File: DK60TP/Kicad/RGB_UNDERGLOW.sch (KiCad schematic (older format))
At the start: 0 parts

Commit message: - DK60TP: Added RGB underglow
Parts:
- added C12, C13, C14, C15, C16: 0.1u, Capacitors_SMD:C_0805_HandSoldering, symbol C_Small
- added D149, D150, D151, D152, D153: WS2812B, Footprint:WS2812B, symbol WS2812B
- added J2: 3PIN, Pin_Headers:Pin_Header_Straight_1x03, symbol 3PIN
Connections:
- new net: D149.2 (DOUT), D150.4 (DIN)
- new net: D150.2 (DOUT), D151.4 (DIN)
- new net: D151.2 (DOUT), D152.4 (DIN)
- new net: D152.2 (DOUT), D153.4 (DIN)
- new net DOUT: D153.2 (DOUT), J2.3
- new net GND: C12.2, C13.2, C14.2, C15.2, C16.2, D149.3 (VSS), D150.3 (VSS), D151.3 (VSS), D152.3 (VSS), D153.3 (VSS), J2.2
- new net RGB: D149.4 (DIN)
- new net VCC: C12.1, C13.1, C14.1, C15.1, C16.1, D149.1 (VDD), D150.1 (VDD), D151.1 (VDD), D152.1 (VDD), D153.1 (VDD), J2.1

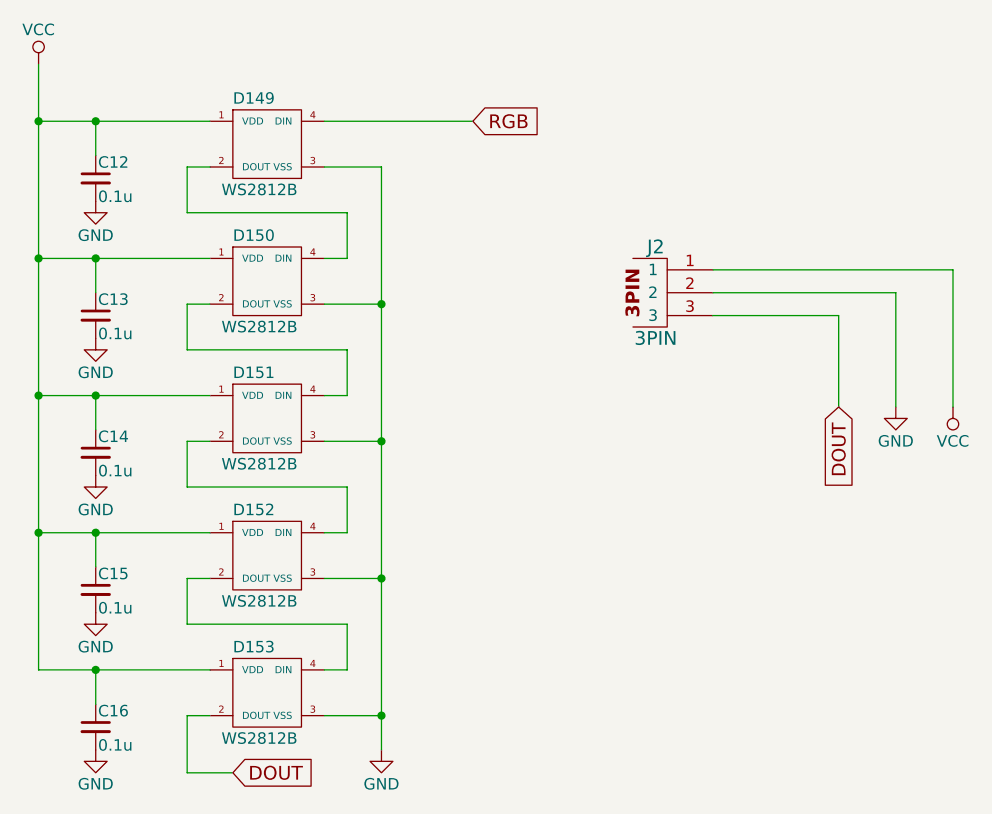
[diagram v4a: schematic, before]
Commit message: - DK60TP: Added RGB underglow on Mouse PCB
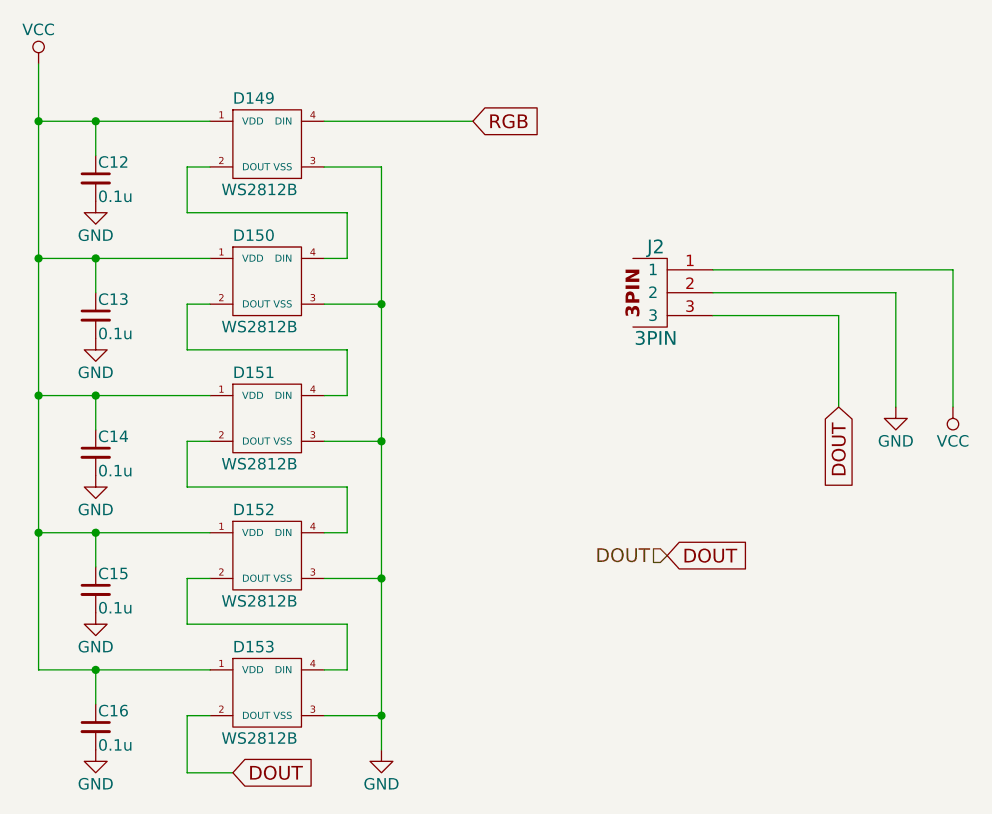
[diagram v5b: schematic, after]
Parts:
- J2: footprint Pin_Headers:Pin_Header_Straight_1x03 -> Pin_Headers:Pin_Header_Angled_1x03
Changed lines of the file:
@@
 LIBS:keyboard_parts
 LIBS:mkl27z256vfm4
+LIBS:TS65
 LIBS:DK60TP-cache
 EELAYER 25 0
@@
 $EndDescr
 $Comp
-L VCC #PWR20
+L VCC #PWR020
 U 1 1 593558DB
 P 1700 1100
-F 0 "#PWR20" H 1700 950 50  0001 C CNN
+F 0 "#PWR020" H 1700 950 50  0001 C CNN
 F 1 "VCC" H 1700 1250 50  0000 C CNN
 F 2 "" H 1700 1100 50  0000 C CNN
@@
 $EndComp
 $Comp
-L GND #PWR26
+L GND #PWR021
 U 1 1 59355E8A
 P 3200 4100
-F 0 "#PWR26" H 3200 3850 50  0001 C CNN
+F 0 "#PWR021" H 3200 3850 50  0001 C CNN
 F 1 "GND" H 3200 3950 50  0000 C CNN
 F 2 "" H 3200 4100 50  0000 C CNN
@@
 $EndComp
 $Comp
-L GND #PWR21
+L GND #PWR022
 U 1 1 59356713
 P 1950 1700
-F 0 "#PWR21" H 1950 1450 50  0001 C CNN
+F 0 "#PWR022" H 1950 1450 50  0001 C CNN
 F 1 "GND" H 1950 1550 50  0000 C CNN
 F 2 "" H 1950 1700 50  0000 C CNN
@@
 $EndComp
 $Comp
-L GND #PWR22
+L GND #PWR023
 U 1 1 59356739
 P 1950 2300
-F 0 "#PWR22" H 1950 2050 50  0001 C CNN
+F 0 "#PWR023" H 1950 2050 50  0001 C CNN
 F 1 "GND" H 1950 2150 50  0000 C CNN
 F 2 "" H 1950 2300 50  0000 C CNN
@@
 $EndComp
 $Comp
-L GND #PWR23
+L GND #PWR024
 U 1 1 5935675F
 P 1950 2900
-F 0 "#PWR23" H 1950 2650 50  0001 C CNN
+F 0 "#PWR024" H 1950 2650 50  0001 C CNN
 F 1 "GND" H 1950 2750 50  0000 C CNN
 F 2 "" H 1950 2900 50  0000 C CNN
@@
 $EndComp
 $Comp
-L GND #PWR24
+L GND #PWR025
 U 1 1 59356785
 P 1950 3500
-F 0 "#PWR24" H 1950 3250 50  0001 C CNN
+F 0 "#PWR025" H 1950 3250 50  0001 C CNN
 F 1 "GND" H 1950 3350 50  0000 C CNN
 F 2 "" H 1950 3500 50  0000 C CNN
@@
 F 0 "J2" H 4400 2300 60  0000 C CNN
 F 1 "3PIN" H 4400 1900 60  0000 C CNN
-F 2 "Pin_Headers:Pin_Header_Straight_1x03" H 4450 2100 60  0001 C CNN
+F 2 "Pin_Headers:Pin_Header_Angled_1x03" H 4450 2100 60  0001 C CNN
 F 3 "" H 4450 2100 60  0000 C CNN
 	1    4450 2100
@@
 $EndComp
 $Comp
-L VCC #PWR28
+L VCC #PWR026
 U 1 1 59356ADE
 P 5700 2600
-F 0 "#PWR28" H 5700 2450 50  0001 C CNN
+F 0 "#PWR026" H 5700 2450 50  0001 C CNN
 F 1 "VCC" H 5700 2750 50  0000 C CNN
 F 2 "" H 5700 2600 50  0000 C CNN
@@
 $EndComp
 $Comp
-L GND #PWR27
+L GND #PWR027
 U 1 1 59356B44
 P 5450 2600
-F 0 "#PWR27" H 5450 2350 50  0001 C CNN
+F 0 "#PWR027" H 5450 2350 50  0001 C CNN
 F 1 "GND" H 5450 2450 50  0000 C CNN
 F 2 "" H 5450 2600 50  0000 C CNN
@@
 Connection ~ 1950 3750
 $Comp
-L GND #PWR25
+L GND #PWR028
 U 1 1 59357568
 P 1950 4100
-F 0 "#PWR25" H 1950 3850 50  0001 C CNN
+F 0 "#PWR028" H 1950 3850 50  0001 C CNN
 F 1 "GND" H 1950 3950 50  0000 C CNN
 F 2 "" H 1950 4100 50  0000 C CNN
@@
 	1    0    0    -1
 $EndComp
+Text HLabel 4450 3250 0    60   Input ~ 0
+DOUT
+Text GLabel 4450 3250 2    60   Input ~ 0
+DOUT
 $EndSCHEMATC

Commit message: - DK60TP: Updated routing
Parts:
- J2: footprint Pin_Headers:Pin_Header_Angled_1x03 -> Connectors_Molex:Molex_PicoBlade_53048-0310_03x1.25mm_Angled
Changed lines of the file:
@@
 F 0 "J2" H 4400 2300 60  0000 C CNN
 F 1 "3PIN" H 4400 1900 60  0000 C CNN
-F 2 "Pin_Headers:Pin_Header_Angled_1x03" H 4450 2100 60  0001 C CNN
+F 2 "Connectors_Molex:Molex_PicoBlade_53048-0310_03x1.25mm_Angled" H 4450 2100 60  0001 C CNN
 F 3 "" H 4450 2100 60  0000 C CNN
 	1    4450 2100

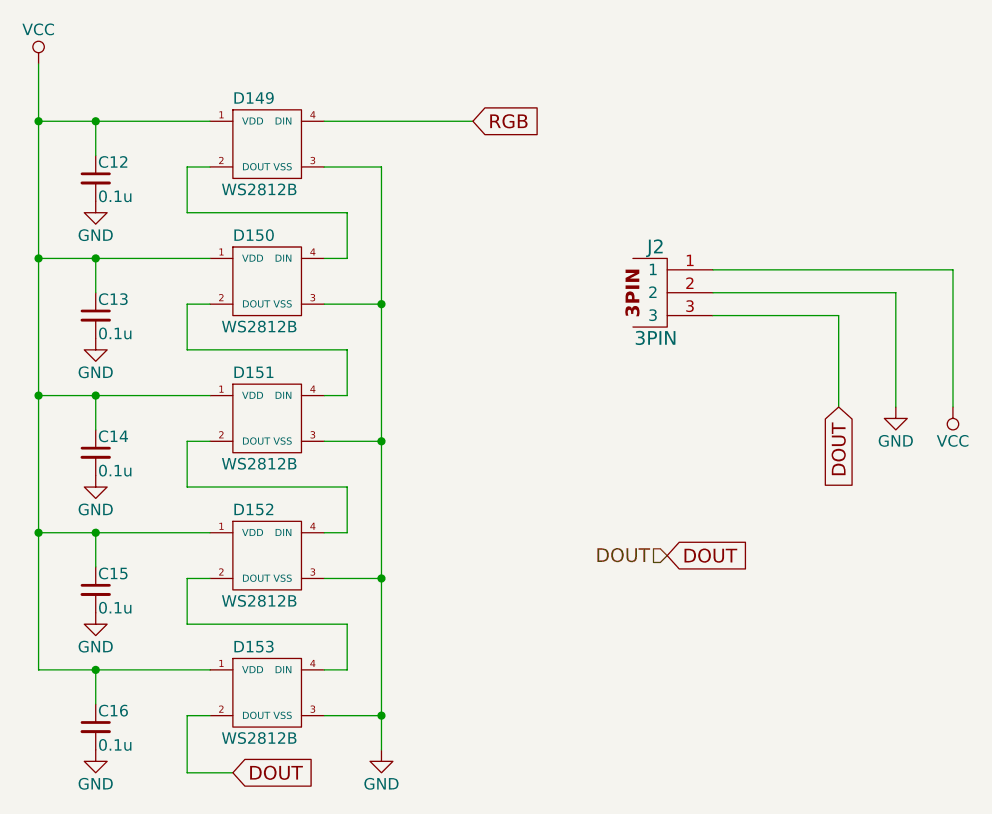
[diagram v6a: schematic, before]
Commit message: - DK60TP: Updated Crystal position - DK60TP: Fixed labels for connectors - DK60TP: Updated routing
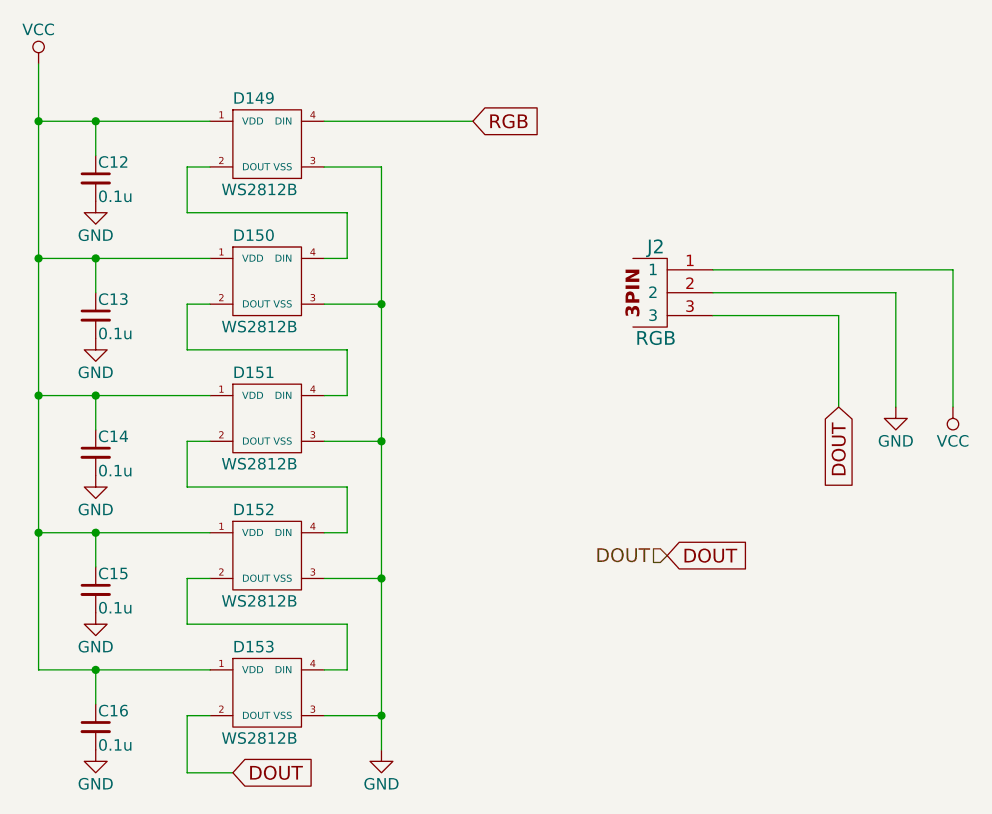
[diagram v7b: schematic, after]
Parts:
- J2: value 3PIN -> RGB
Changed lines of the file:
@@
 P 4450 2100
 F 0 "J2" H 4400 2300 60  0000 C CNN
-F 1 "3PIN" H 4400 1900 60  0000 C CNN
+F 1 "RGB" H 4400 1900 60  0000 C CNN
 F 2 "Connectors_Molex:Molex_PicoBlade_53048-0310_03x1.25mm_Angled" H 4450 2100 60  0001 C CNN
 F 3 "" H 4450 2100 60  0000 C CNN
